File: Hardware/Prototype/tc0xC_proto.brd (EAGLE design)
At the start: 101.6 x 98.8 mm, 101 parts, among them IC1 AP2112M-3.3TRG1, Q1 2.5A/30V, Q2 MBT3904DW1T1, Q3 600mA/40V, Q4 MBT3904DW1T1, U2 ESP3212, U4 FT231XS, U5 W25Q32FVSS, Y1 26MHz, Y2 32.768kHz

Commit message: routed
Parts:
- removed S1: PTS526, IDEO-Switches:5.20MM_SPST_MOM
- moved C32 60.5 mm to (3.01, 24.8), flipped to the bottom, turned to 270 degrees
- moved TP1 59.6 mm to (3.12, 27.2), flipped to the bottom
- moved R19 56.1 mm to (19.3, 50.2)
- moved R11 54.6 mm to (11.3, 43.1), turned to 180 degrees
- moved R10 46.9 mm to (16.3, 38.7)
- moved C34 45.8 mm to (4.91, 20.3)
- moved R8 40.3 mm to (7.17, 31.7)
- moved C33 37.9 mm to (4.90, 21.9)
- moved R6 37.7 mm to (5.46, 30.2), turned to 0 degrees
- moved C35 26.0 mm to (19.7, 39.3)
- moved C27 25.1 mm to (24.5, 19.7)
- moved C24 22.7 mm to (40.8, 35.5), turned to 0 degrees
- moved R1 21.9 mm to (42.0, 22.7)
- moved R2 21.6 mm to (24.5, 21.3)
- moved C5 20.4 mm to (24.5, 18.2)
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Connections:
- removed net CA8: U1.28
- removed net CA9: U1.1
- removed net RX_IN: U2.27
- removed net TX_IN: U2.25
- removed net XMARK: U2.38
- net CHIP_PU: now also S3.2; no longer S1.P$3, S1.P$4
- net GND: now also S3.1, S3.3; no longer S1.P$1, S1.P$2
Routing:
- net CA4: track 0.00 -> 188.8 mm, vias 0 -> 5
- net CA3: track 0.00 -> 146.1 mm, vias 0 -> 6
- net CA1: track 0.00 -> 135.2 mm, vias 0 -> 8
- net IR_OUT: track 0.00 -> 125.3 mm, vias 0 -> 5
- net CA2: track 0.00 -> 124.2 mm, vias 0 -> 6
- net 3.3V: track 0.00 -> 97.3 mm, vias 0 -> 8
- net CHIP_PU: track 0.00 -> 56.0 mm, vias 0 -> 3
- net BUZZER_OUT: track 0.00 -> 51.2 mm, vias 0 -> 2
- net DST: track 0.00 -> 50.2 mm, vias 0 -> 2
- net U0TXD: track 0.00 -> 42.8 mm, vias 0 -> 2
- net SDA: track 0.00 -> 37.7 mm, vias 0 -> 4
- net U0RXD: track 0.00 -> 36.9 mm, vias 0 -> 2
- net ACC_INT: track 0.00 -> 36.1 mm, vias 0 -> 2
- net FLASH_SCS: track 0.00 -> 33.2 mm, vias 0 -> 2
- net FLASH_VDD: track 0.00 -> 33.1 mm
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
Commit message: routed
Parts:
- added TP2, TP3: TPSTP08R, testpad:TP08R
- C6: value 4.7uF -> 0.1uF
- moved C23 6.93 mm to (47.2, 28.5)
- moved C6 0.94 mm to (49.4, 44.8), turned to 0 degrees
- moved R4 0.74 mm to (33.3, 31.3)
- moved R3 0.59 mm to (33.1, 32.6)
- moved R6 0.59 mm to (4.91, 30.4)
- moved R8 0.45 mm to (7.57, 31.9)
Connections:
- removed net T_B: Q4.6, U2.23
- new net T_B1: TP2.TP, U2.23
- new net T_B2: Q4.6, TP3.TP
- net 3.3V: now also C6.2; no longer C6.1
- net GND: now also C6.1; no longer C6.2
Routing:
- net 3.3V: track 97.3 -> 241.1 mm, vias 8 -> 18
- net CA3: track 146.1 -> 269.0 mm, vias 6 -> 12
- net CA2: track 124.2 -> 245.3 mm, vias 6 -> 17
- net CA4: track 188.8 -> 309.6 mm, vias 5 -> 10
- net CA5: track 27.9 -> 121.7 mm, vias 0 -> 6
- net CA6: track 19.0 -> 93.4 mm, vias 0 -> 4
- net CA1: track 135.2 -> 205.9 mm, vias 8 -> 16
- net N$16: track 0.00 -> 62.7 mm, vias 0 -> 1
- net CA7: track 26.3 -> 85.9 mm, vias 0 -> 4
- net T_SELECT: track 0.00 -> 56.2 mm, vias 0 -> 3
- net GND: track 0.88 -> 26.4 mm, vias 0 -> 20
- net SCL: track 12.0 -> 35.0 mm, vias 3 -> 6
- net N$13: track 2.28 -> 10.5 mm, vias 0 -> 2
- net N$3: track 2.23 -> 5.09 mm
- net V_USB: track 25.4 -> 27.8 mm
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- added copper zone on layer 1, net GND
- added copper zone on layer 16, net GND
- added copper zone on layer 16, net T_SELECT
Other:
- board size 101.6 x 98.8 mm -> 101.6 x 99.6 mm

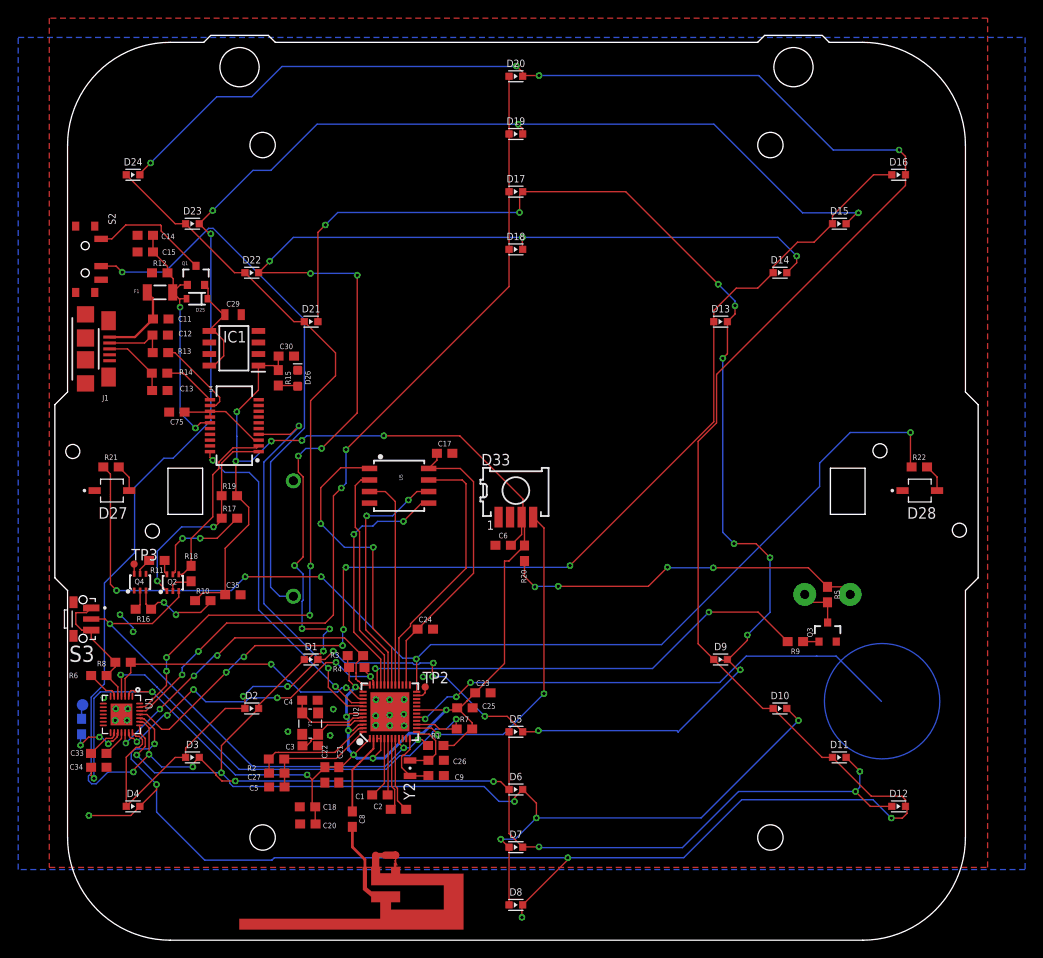
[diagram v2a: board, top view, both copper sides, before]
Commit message: routed with polys
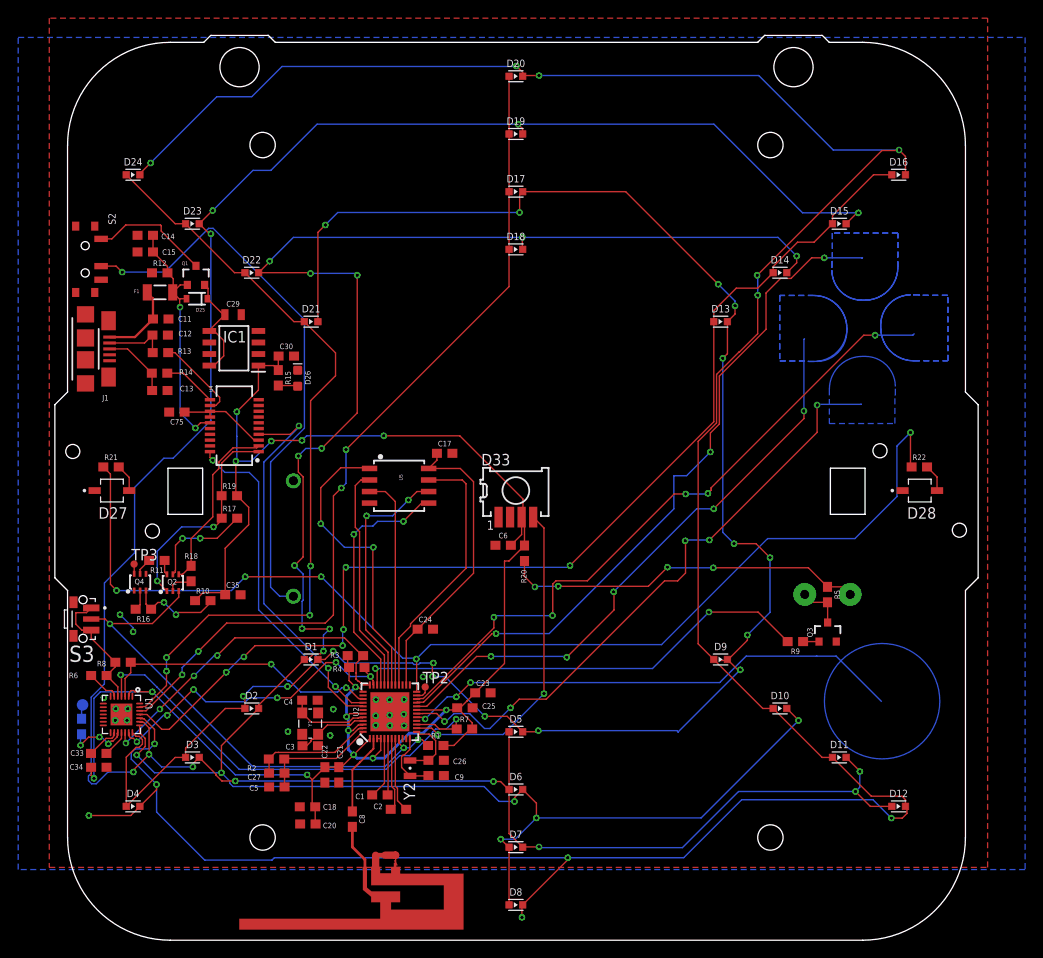
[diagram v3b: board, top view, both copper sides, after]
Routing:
- net T_UP: track 0.00 -> 78.2 mm, vias 0 -> 3
- net T_LEFT: track 0.00 -> 74.3 mm, vias 0 -> 5
- net T_DOWN: track 0.00 -> 69.0 mm, vias 0 -> 5
- net T_RIGHT: track 0.00 -> 65.9 mm, vias 0 -> 5
- net CA4: track 309.6 -> 313.2 mm, vias 10 -> 12
- net IR_OUT: track 125.3 -> 127.1 mm
- added copper zone on layer 16, net T_DOWN
- added copper zone on layer 16, net T_LEFT
- added copper zone on layer 16, net T_RIGHT
- added copper zone on layer 16, net T_UP

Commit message: adjust LED placement. adjust hole and dimension placement.
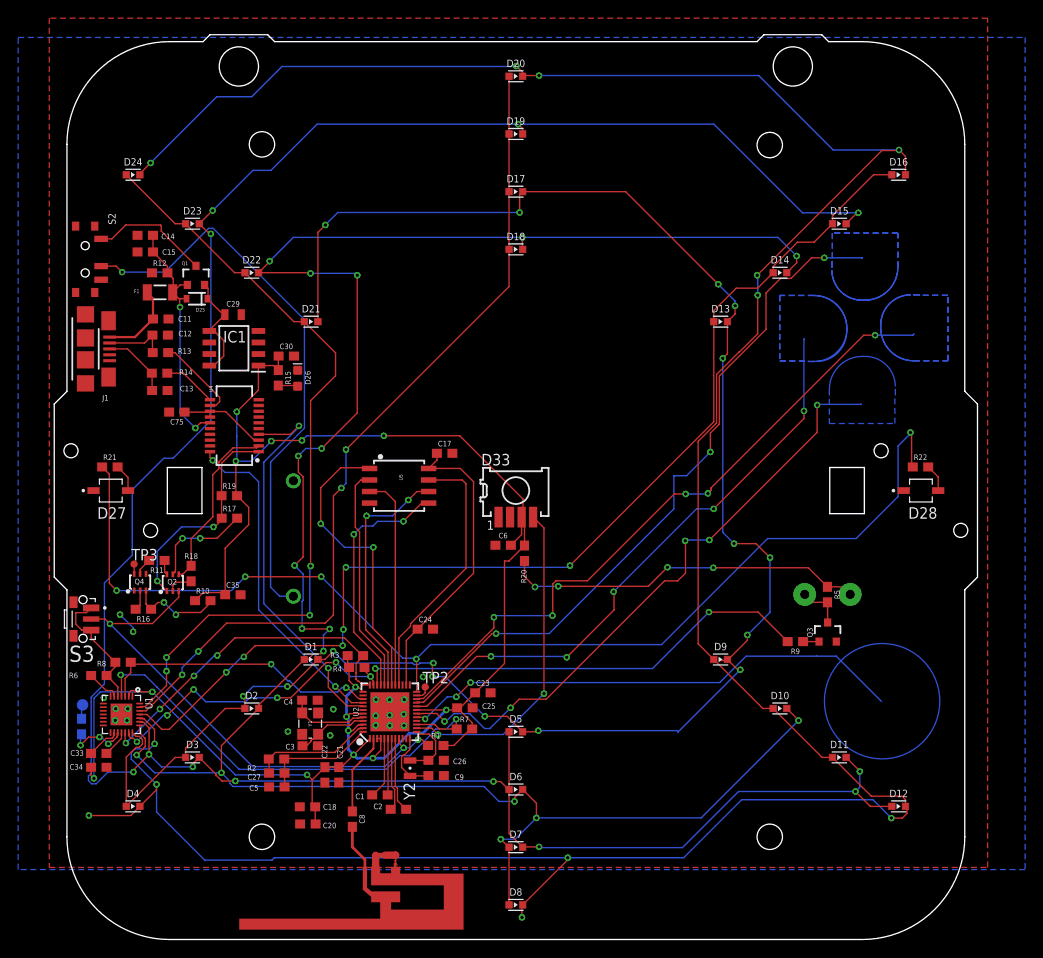
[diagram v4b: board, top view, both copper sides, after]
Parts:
- moved D27 0.13 mm to (6.22, 50.8)
- moved R21 0.13 mm to (6.12, 53.4)
- moved D28 0.13 mm to (95.4, 50.8)
- moved R22 0.13 mm to (95.3, 53.4)

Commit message: adjust dimensions for better fitting for plastics
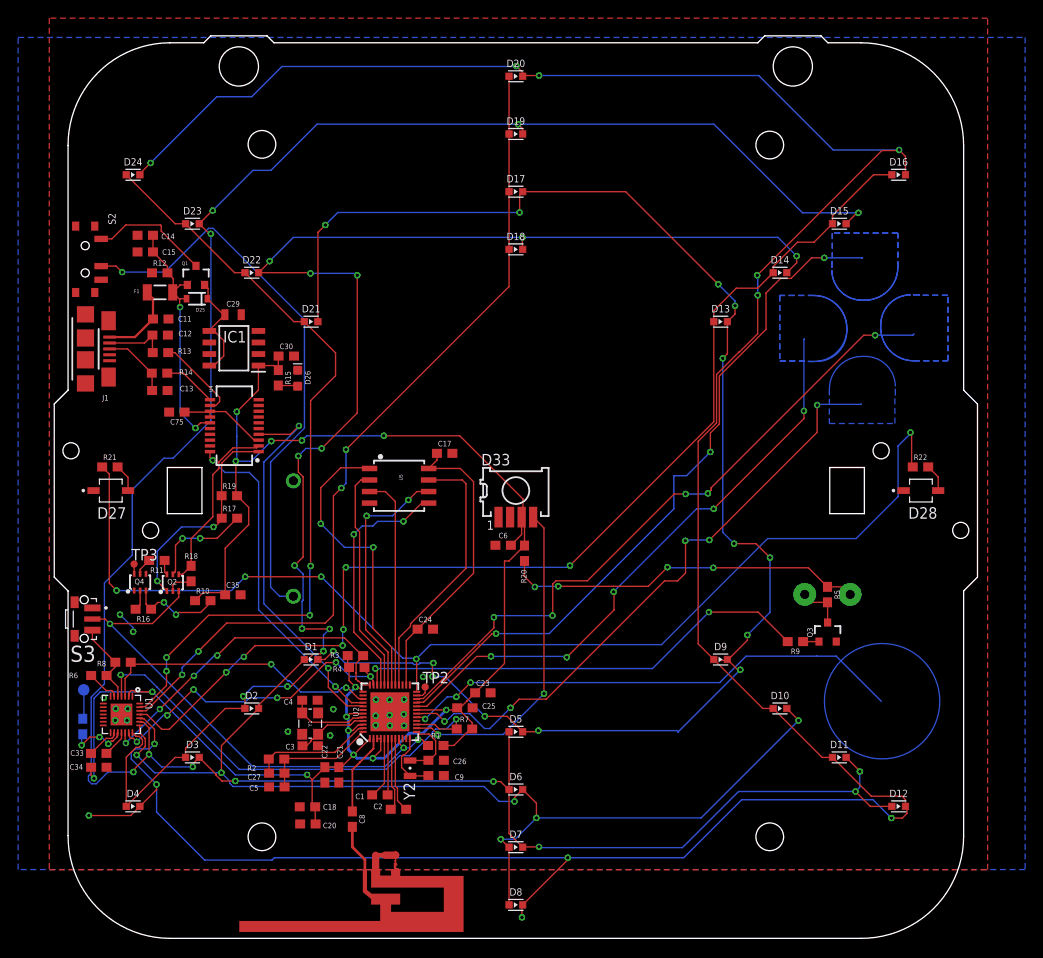
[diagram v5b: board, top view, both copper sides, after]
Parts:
- moved TP1 1.66 mm to (3.24, 28.9)
- moved E1 0.25 mm to (34.2, 9.14)
- moved C32 0.13 mm to (3.14, 24.8)
- moved S3 0.13 mm to (3.30, 36.7)
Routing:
- net GND: track 26.4 -> 21.7 mm
- net AUDIO_IN: track 1.58 -> 3.25 mm
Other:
- board size 101.6 x 99.6 mm -> 101.6 x 99.3 mm
